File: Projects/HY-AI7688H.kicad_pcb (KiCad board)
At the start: 2 copper layers, 100 x 85 mm, 291 parts, among them J1 CONN_SMA, P1 USB_OTG, P10 CONN_01X04, P2 USB_A, P3 HR911102A, P4 CONN_01X14, P5 CONN_01X12, P6 CONN_01X04, P7 CONN_01X16, P8 CONN_02X05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

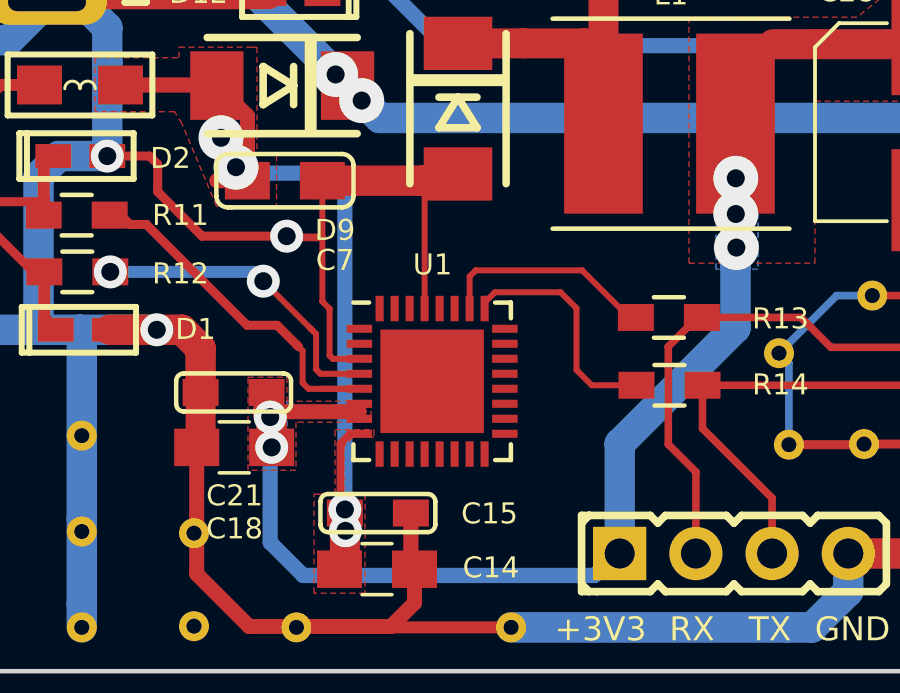
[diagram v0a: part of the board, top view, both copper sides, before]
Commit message: fix footprint cp2102
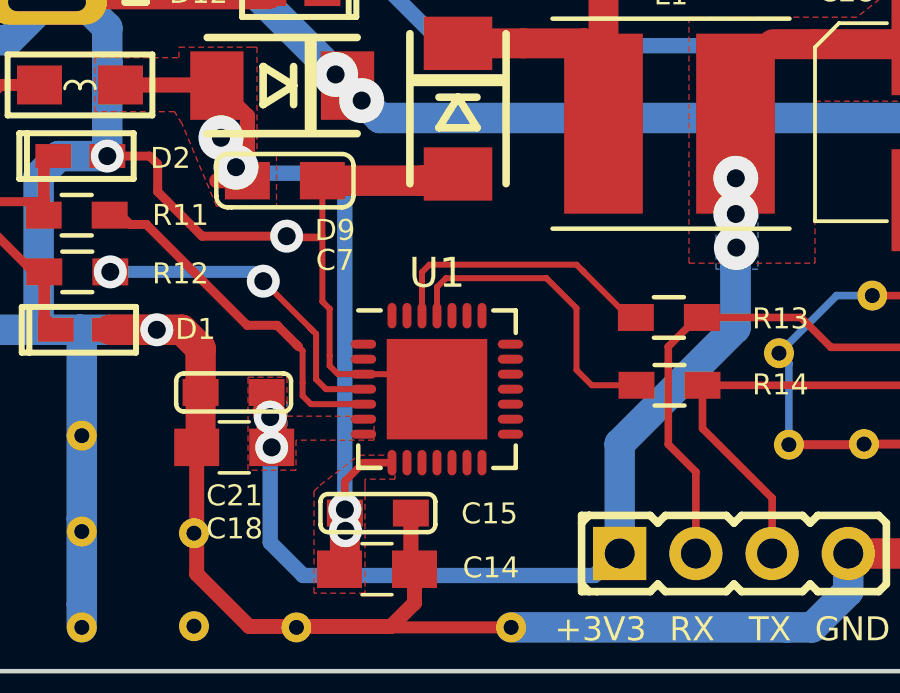
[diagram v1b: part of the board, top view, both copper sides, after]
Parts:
- U1: footprint nhantt-kicad-lib:QFN-32-1EP_5x5mm_Pitch0.5mm -> Housings_DFN_QFN:QFN-28-1EP_5x5mm_Pitch0.5mm
- moved U1 0.31 mm to (94.2, 110.6)
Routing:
- net +3V3: track 392.5 -> 389.0 mm
- net Net-(R13-Pad2): track 7.35 -> 10.5 mm
- net Net-(R14-Pad2): track 7.90 -> 10.4 mm
- net GND: track 1422.5 -> 1420.6 mm
- net /AI7688H/D-: track 12.7 -> 12.0 mm
- net /AI7688H/D+: track 10.6 -> 11.1 mm
